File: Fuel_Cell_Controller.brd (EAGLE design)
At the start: 203.2 x 163.8 mm, 115 parts, among them J1 BLUETOOTH, U1 MAX232PTH

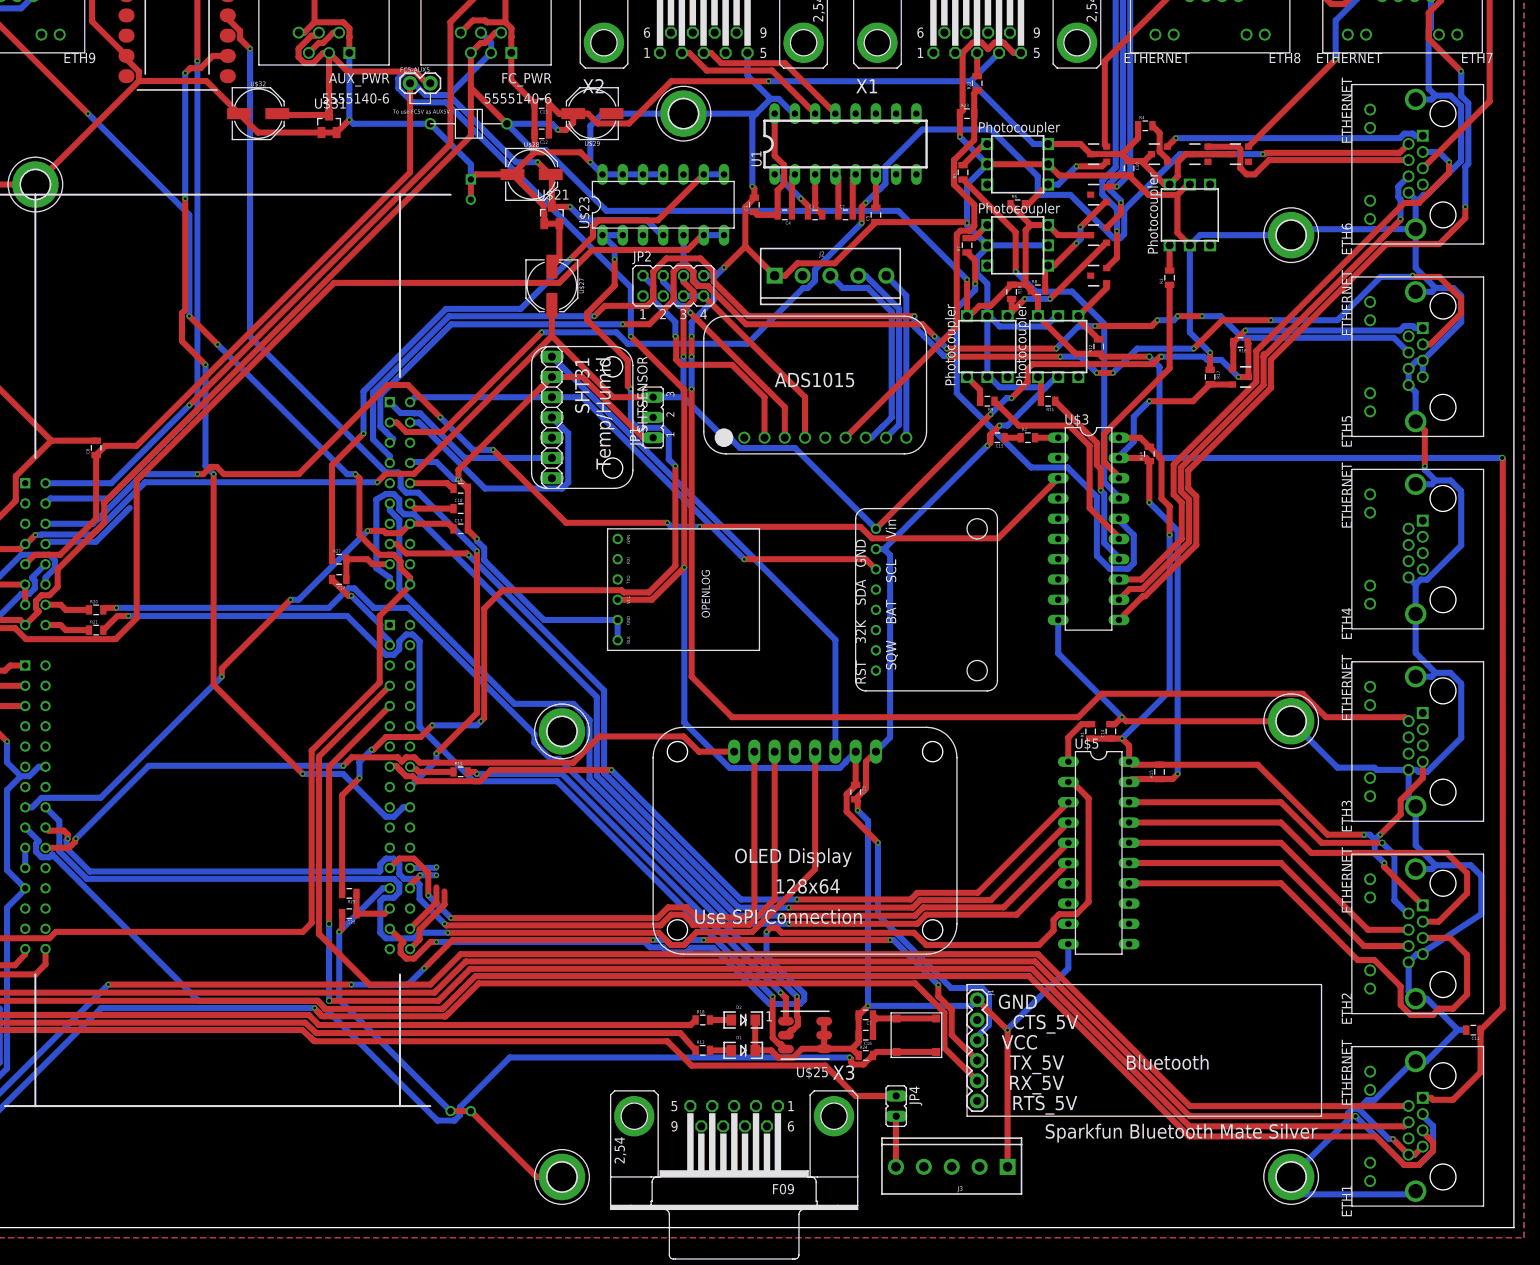
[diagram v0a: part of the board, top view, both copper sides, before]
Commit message: Labelled RJ45 Connectors
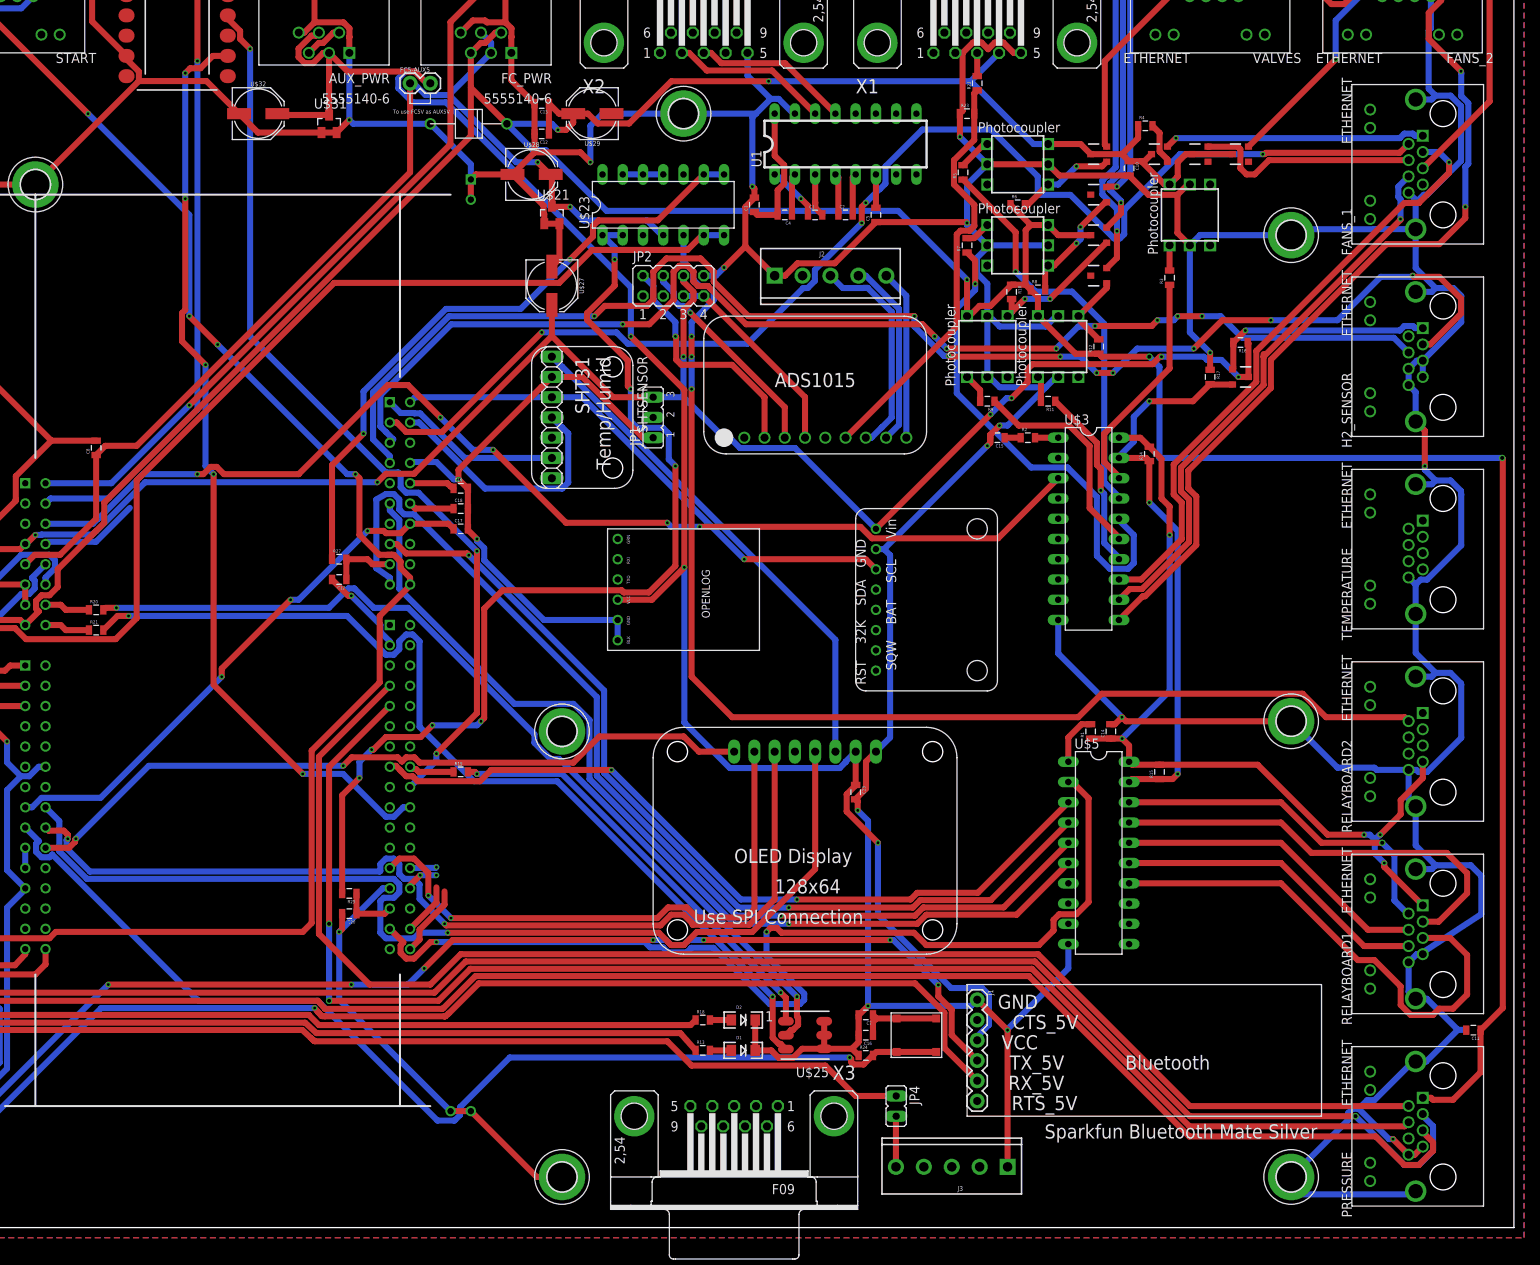
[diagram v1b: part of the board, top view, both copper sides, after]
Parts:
- renumbered ETH1 to PRESSURE, ETH2 to RELAYBOARD1, ETH3 to RELAYBOARD2, ETH4 to TEMPERATURE, ETH5 to H2_SENSOR, ETH6 to FANS_1, ETH7 to FANS_2, ETH8 to VALVES, ETH9 to START
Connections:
- net GND: no longer U$23.14
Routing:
- net GND: track 1328.3 -> 1323.6 mm

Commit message: Added PWR indicator LEDS
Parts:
- added AUX12V, AUX5V, FC12V, FC5V: (no value), led:CHIP-LED0805
- added R28, R29, R30, R31, R32, R33, R34, R35, R36, R37: (no value), resistor:R0805
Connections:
- new net N$21: FC5V.A, R28.1
- new net N$23: FC12V.A, R29.1
- new net N$25: AUX5V.A, R30.1
- new net N$28: AUX12V.A, R31.1
- new net _CAP_CURR: R36.1, RELAYBOARD2.P$6
- new net _FC_CURR: R32.1, RELAYBOARD2.P$4
- new net _MOTOR_CURR: R34.1, RELAYBOARD2.P$5
- net AUX12V: now also R31.2, R6.1, U$12.D, U$6.VCC
- net AUX5V: now also R30.2
- net CAP_CURR: now also R36.2, R37.1; no longer RELAYBOARD2.P$6
- net FC12V: now also R29.2; no longer R6.1, U$12.D, U$6.VCC
- net FC5V: now also R28.2
- net FC_CURR: now also R32.2, R33.1; no longer RELAYBOARD2.P$4
- net GND: now also AUX12V.C, AUX5V.C, FANS_1.P$7, FANS_2.P$6, FANS_2.P$7, FC12V.C, FC5V.C, R33.2, R35.2, R37.2
- net MOTOR_CURR: now also R34.2, R35.1; no longer RELAYBOARD2.P$5
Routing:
- net FC12V: track 497.3 -> 482.1 mm

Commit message: Deleted Start Screw Terminal
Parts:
- removed J3: (no value), SparkFun-Connectors:SCREWTERMINAL-3.5MM-5
- removed JP4: (no value), jumper:JP1
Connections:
- removed net START: J3.5, JP4.2
- net GND: no longer J3.1
- net _START: no longer JP4.1
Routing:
- net GND: track 1323.6 -> 1306.4 mm
- net START: track 6.36 -> 0.00 mm
- net _START: track 323.8 -> 318.7 mm
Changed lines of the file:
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@@
 <element name="R22" library="SparkFun-Passives" package="0805" value="1kΩ" x="135.89" y="143.51" rot="R90"/>
 <element name="R23" library="SparkFun-Passives" package="0805" value="1kΩ" x="134.62" y="139.7"/>
-<element name="J3" library="SparkFun-Connectors" library_urn="urn:adsk.eagle:library:513" package="SCREWTERMINAL-3.5MM-5" package3d_urn="urn:adsk.eagle:package:38112/1" value="" x="139.7" y="7.62" rot="R180">
-<attribute name="PROD_ID" value="Combine 8288+8399" x="139.7" y="7.62" size="1.778" layer="27" rot="R180" display="off"/>
-</element>
 <element name="X3" library="con-subd" library_urn="urn:adsk.eagle:library:189" package="F09HP" package3d_urn="urn:adsk.eagle:package:10232/1" value="" x="105.41" y="13.97" rot="R180">
 <attribute name="MF" value="" x="105.41" y="13.97" size="1.778" layer="27" rot="R180" display="off"/>
@@
 <element name="U$28" library="100uF_Cap" package="PANASONIC_D" value="1µF" x="80.01" y="132.08"/>
 <element name="U$29" library="100uF_Cap" package="PANASONIC_D" value="10µF" x="87.63" y="139.7" rot="R180"/>
-<element name="JP4" library="jumper" library_urn="urn:adsk.eagle:library:252" package="JP1" package3d_urn="urn:adsk.eagle:package:15455/1" value="" x="125.73" y="15.24" rot="R180"/>
 <element name="START" library="ETHERNET" package="A122645-ND" value="ETHERNET" x="13.97" y="158.75" rot="R180"/>
 <element name="C17" library="SparkFun-Capacitors" package="0805" value="" x="71.12" y="87.63"/>
@@
 <contactref element="U$25" pad="4"/>
 <contactref element="R23" pad="1"/>
-<contactref element="J3" pad="1"/>
 <contactref element="C7" pad="2"/>
 <contactref element="C16" pad="2"/>
@@
 <wire x1="14.224" y1="60.96" x2="9.26" y2="65.924" width="0.762" layer="1"/>
 <wire x1="9.26" y1="65.924" x2="9.26" y2="69.85" width="0.762" layer="1"/>
-<wire x1="139.7" y1="7.62" x2="139.7" y2="24.765" width="0.762" layer="1"/>
 <wire x1="139.7" y1="24.765" x2="135.89" y2="28.575" width="0.762" layer="1"/>
 <wire x1="147.32" y1="35.56" x2="147.32" y2="32.512" width="0.762" layer="16"/>
@@
 <wire x1="191.77" y1="130.81" x2="191.8786" y2="129.5226" width="0" layer="19" extent="16-16"/>
 <wire x1="191.77" y1="156.21" x2="193.0574" y2="155.9426" width="0" layer="19" extent="16-16"/>
+<wire x1="75.692" y1="144.306" x2="77.47" y2="143.88" width="0" layer="19" extent="1-1"/>
+<wire x1="79.248" y1="143.29" x2="77.47" y2="143.88" width="0" layer="19" extent="1-1"/>
 <wire x1="190.75" y1="154.43" x2="192.79" y2="154.43" width="0" layer="19" extent="1-1"/>
+<wire x1="58.928" y1="144.306" x2="57.15" y2="147.32" width="0" layer="19" extent="1-1"/>
 <wire x1="91.44" y1="132.08" x2="87.376" y2="133.604" width="0" layer="19" extent="1-1"/>
+<wire x1="52.324" y1="143.798" x2="57.15" y2="147.32" width="0" layer="19" extent="1-1"/>
+<wire x1="29.398" y1="64.008" x2="19.05" y2="57.790715625" width="0" layer="19" extent="1-1"/>
 <wire x1="82.55" y1="106.68" x2="82.55" y2="120.51" width="0" layer="19" extent="1-1"/>
 <wire x1="106.68" y1="99.06" x2="95.25" y2="99.06" width="0" layer="19" extent="1-1"/>
@@
 <wire x1="61.0426" y1="75.6094" x2="74.0664" y2="83.6907625" width="0" layer="19" extent="16-16"/>
 <wire x1="62.23" y1="70.490715625" x2="62.23" y2="73.030715625" width="0" layer="19" extent="1-1"/>
+<wire x1="48.194" y1="83.82" x2="54.98" y2="81.28" width="0" layer="19" extent="1-1"/>
+<wire x1="46.162" y1="87.884" x2="48.194" y2="83.82" width="0" layer="19" extent="1-1"/>
 <wire x1="62.23" y1="55.250715625" x2="62.23" y2="70.490715625" width="0" layer="19" extent="1-1"/>
 <wire x1="64.77" y1="50.170715625" x2="62.23" y2="55.250715625" width="0" layer="19" extent="1-1"/>
 <wire x1="62.23" y1="42.550715625" x2="64.77" y2="50.170715625" width="0" layer="19" extent="1-1"/>
-<wire x1="75.692" y1="144.306" x2="7.62" y2="6.35" width="0" layer="19" extent="1-1"/>
-<wire x1="79.248" y1="143.29" x2="75.692" y2="144.306" width="0" layer="19" extent="1-1"/>
-<wire x1="52.324" y1="143.798" x2="79.248" y2="143.29" width="0" layer="19" extent="1-1"/>
-<wire x1="58.928" y1="144.306" x2="52.324" y2="143.798" width="0" layer="19" extent="1-1"/>
-<wire x1="48.194" y1="83.82" x2="58.928" y2="144.306" width="0" layer="19" extent="1-1"/>
-<wire x1="46.162" y1="87.884" x2="48.194" y2="83.82" width="0" layer="19" extent="1-1"/>
-<wire x1="29.398" y1="64.008" x2="46.162" y2="87.884" width="0" layer="19" extent="1-1"/>
 </signal>
 <signal name="FROM_OPEN">
@@
 <wire x1="68.201525" y1="13.4233125" x2="53.1768375" y2="28.448" width="0.762" layer="16"/>
 </signal>
-<signal name="START">
-<contactref element="J3" pad="5"/>
-<contactref element="JP4" pad="2"/>
-<wire x1="125.7" y1="7.62" x2="125.7" y2="13.94" width="0.762" layer="1"/>
-<wire x1="125.7" y1="13.94" x2="125.73" y2="13.97" width="0.762" layer="1"/>
-</signal>
 <signal name="_START">
-<contactref element="JP4" pad="1"/>
 <contactref element="U$1" pad="PF_12"/>
 <contactref element="START" pad="P$1"/>
-<wire x1="125.73" y1="16.51" x2="120.65" y2="16.51" width="0.762" layer="1"/>
 <wire x1="120.65" y1="16.51" x2="116.84" y2="20.32" width="0.762" layer="1"/>
 <wire x1="116.84" y1="20.32" x2="100.076" y2="20.32" width="0.762" layer="1"/>
